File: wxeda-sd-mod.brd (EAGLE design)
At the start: 101.3 x 40.6 mm, 23 parts, among them U1 SD_CARD, X2 TAPE IN / OUT

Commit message: release
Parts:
- C2, C3, C4, C5: device adafruit:E5-8,5 -> adafruit:E2-5
- moved C3 8.98 mm to (72.4, 24.1), turned to 0 degrees
- moved R7 6.48 mm to (68.6, 16.5), turned to 0 degrees
- moved C2 1.80 mm to (85.1, 24.1)
- moved C5 1.80 mm to (92.7, 24.1)
- moved C4 1.27 mm to (64.8, 24.1), turned to 0 degrees
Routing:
- net Y_OUT: track 16.7 -> 11.4 mm
- net N$8: track 12.7 -> 8.25 mm
- net DSE: track 40.1 -> 44.2 mm
- net N$7: track 8.89 -> 5.05 mm
- net N$4: track 11.3 -> 9.23 mm
- net A_IN: track 15.2 -> 16.8 mm
- net C_OUT: track 9.73 -> 11.1 mm
- net N$6: track 11.2 -> 10.2 mm
- net GREEN: track 26.5 -> 25.4 mm
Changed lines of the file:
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@@
 <elements>
 <element name="JP1" library="pinhead" package="1X06" value="7SEG_LR" x="45.72" y="30.48" smashed="yes">
-<attribute name="NAME" x="49.4538" y="27.2288" size="1.27" layer="25" ratio="10"/>
+<attribute name="NAME" x="39.2938" y="27.2288" size="0.8128" layer="25" ratio="10"/>
 </element>
 <element name="JP2" library="pinhead" package="1X03" value="IRDA" x="77.47" y="35.56" smashed="yes" rot="R180"/>
 <element name="U1" library="SparkFun-Connectors" package="SDCARD_4UCONN" value="SD_CARD" x="21.59" y="11.43" smashed="yes" rot="R90">
-<attribute name="VALUE" x="17.54" y="22.13" size="1.27" layer="27" ratio="10"/>
+<attribute name="VALUE" x="8.65" y="13.24" size="0.8128" layer="27" ratio="10"/>
 </element>
 <element name="JP3" library="pinhead" package="1X06" value="7SEG_HR" x="45.72" y="38.1" smashed="yes"/>
@@
 <attribute name="NAME" x="43.18" y="11.43" size="0.8128" layer="25" font="vector" rot="R180"/>
 </element>
-<element name="C2" library="adafruit" package="E5-8,5" value="10uF" x="83.82" y="22.86" smashed="yes" rot="R180">
-<attribute name="NAME" x="84.7598" y="18.034" size="1.27" layer="25" ratio="10" rot="R180"/>
-<attribute name="VALUE" x="86.3346" y="25.8826" size="1.27" layer="27" ratio="10" rot="R180"/>
+<element name="C2" library="adafruit" package="E2-5" value="10uF" x="85.09" y="24.13" smashed="yes" rot="R180">
+<attribute name="NAME" x="87.2998" y="20.574" size="0.8128" layer="25" ratio="10" rot="R180"/>
 </element>
 <element name="R9" library="SparkFun-Passives" package="AXIAL-0.3" value="75" x="55.88" y="26.67" smashed="yes">
-<attribute name="NAME" x="53.34" y="29.2354" size="0.8128" layer="25" rot="R270"/>
-</element>
-<element name="C4" library="adafruit" package="E5-8,5" value="47uF" x="66.04" y="24.13" smashed="yes" rot="R90">
-<attribute name="NAME" x="63.754" y="23.1902" size="1.27" layer="25" ratio="10" rot="R90"/>
-<attribute name="VALUE" x="69.0626" y="21.6154" size="1.27" layer="27" ratio="10" rot="R90"/>
-</element>
-<element name="X2" library="adafruit" package="STX3100" value="TAPE IN / OUT" x="88.9" y="40.64" smashed="yes" rot="R270">
-<attribute name="VALUE" x="82.45" y="27.86" size="1.27" layer="27" ratio="10"/>
-</element>
-<element name="C5" library="adafruit" package="E5-8,5" value="10uF" x="93.98" y="22.86" smashed="yes" rot="R180">
-<attribute name="NAME" x="94.9198" y="18.034" size="1.27" layer="25" ratio="10" rot="R180"/>
-<attribute name="VALUE" x="96.4946" y="25.8826" size="1.27" layer="27" ratio="10" rot="R180"/>
-</element>
-<element name="R7" library="SparkFun-Passives" package="AXIAL-0.3" value="75" x="62.23" y="15.24" rot="R270"/>
-<element name="C3" library="adafruit" package="E5-8,5" value="47uF" x="73.66" y="15.24" rot="R90"/>
+<attribute name="NAME" x="57.15" y="24.1554" size="0.8128" layer="25"/>
+</element>
+<element name="C4" library="adafruit" package="E2-5" value="47uF" x="64.77" y="24.13" smashed="yes">
+<attribute name="NAME" x="67.6402" y="21.336" size="0.8128" layer="25" rot="R180"/>
+</element>
+<element name="X2" library="adafruit" package="STX3100" value="TAPE IN / OUT" x="88.9" y="40.64" smashed="yes" rot="R270"/>
+<element name="C5" library="adafruit" package="E2-5" value="10uF" x="92.71" y="24.13" smashed="yes" rot="R180">
+<attribute name="NAME" x="94.9198" y="20.574" size="0.8128" layer="25" ratio="10" rot="R180"/>
+</element>
+<element name="R7" library="SparkFun-Passives" package="AXIAL-0.3" value="75" x="68.58" y="16.51" smashed="yes">
+<attribute name="NAME" x="69.85" y="13.97" size="0.8128" layer="25" font="vector"/>
+</element>
+<element name="C3" library="adafruit" package="E2-5" value="47uF" x="72.39" y="24.13" smashed="yes">
+<attribute name="NAME" x="74.93" y="21.336" size="0.8128" layer="25" ratio="10" rot="R180"/>
+</element>
 <element name="U$1" library="connectors-digital" package="MINIDIN_4_3GND" value="S-VIDEO" x="63.5" y="43.18">
 <attribute name="PACKAGE" value="SHIELDED" x="63.5" y="43.18" size="1.778" layer="27" display="off"/>
@@
 <wire x1="58.42" y1="7.62" x2="58.42" y2="11.43" width="1.016" layer="1"/>
 <wire x1="58.42" y1="11.43" x2="58.42" y2="13.97" width="1.016" layer="1"/>
-<wire x1="58.42" y1="13.97" x2="58.42" y2="15.24" width="0" layer="19" extent="1-16"/>
 <wire x1="58.42" y1="13.97" x2="58.42" y2="16.51" width="1.016" layer="1"/>
 <wire x1="58.42" y1="16.51" x2="58.42" y2="19.05" width="1.016" layer="1"/>
@@
 <wire x1="54.61" y1="13.97" x2="58.42" y2="13.97" width="0.8128" layer="1"/>
 <wire x1="52.07" y1="11.43" x2="58.42" y2="11.43" width="0.8128" layer="1"/>
-<wire x1="62.23" y1="15.24" x2="58.42" y2="15.24" width="0" layer="19" extent="1-16"/>
 <wire x1="74.93" y1="35.56" x2="74.93" y2="33.02" width="1.016" layer="1"/>
 <wire x1="74.93" y1="33.02" x2="77.47" y2="30.48" width="1.016" layer="1"/>
@@
 <contactref element="JP1" pad="1"/>
 <contactref element="R7" pad="P$1"/>
-<wire x1="62.23" y1="19.05" x2="59.69" y2="22.86" width="0.6096" layer="1"/>
-<wire x1="59.69" y1="22.86" x2="55.88" y2="22.86" width="0.6096" layer="1"/>
+<wire x1="64.77" y1="16.51" x2="60.96" y2="22.86" width="0.6096" layer="1"/>
+<wire x1="60.96" y1="22.86" x2="55.88" y2="22.86" width="0.6096" layer="1"/>
 <wire x1="55.88" y1="22.86" x2="55.88" y2="34.29" width="0.6096" layer="1"/>
 <wire x1="55.88" y1="34.29" x2="39.37" y2="34.29" width="0.6096" layer="1"/>
@@
 <contactref element="C5" pad="+"/>
 <wire x1="99.06" y1="35.56" x2="96.52" y2="35.56" width="0.8128" layer="1"/>
-<wire x1="96.52" y1="35.56" x2="96.52" y2="22.86" width="0.8128" layer="1"/>
+<wire x1="96.52" y1="35.56" x2="96.52" y2="24.13" width="0.6096" layer="1"/>
+<wire x1="96.52" y1="24.13" x2="93.726" y2="24.13" width="0.6096" layer="1"/>
 </signal>
 <signal name="GREEN">
 <contactref element="JP4" pad="3"/>
 <contactref element="C2" pad="+"/>
-<wire x1="86.36" y1="22.86" x2="88.9" y2="20.32" width="0.8128" layer="1"/>
-<wire x1="88.9" y1="20.32" x2="99.06" y2="20.32" width="0.8128" layer="1"/>
-<wire x1="99.06" y1="20.32" x2="99.06" y2="33.02" width="0.8128" layer="1"/>
+<wire x1="86.106" y1="24.13" x2="88.646" y2="21.59" width="0.6096" layer="1"/>
+<wire x1="88.646" y1="21.59" x2="99.06" y2="21.59" width="0.6096" layer="1"/>
+<wire x1="99.06" y1="21.59" x2="99.06" y2="33.02" width="0.6096" layer="1"/>
 </signal>
 <signal name="N$1">
@@
 <contactref element="C2" pad="-"/>
 <wire x1="83.7" y1="32.94" x2="83.82" y2="32.94" width="0.6096" layer="1"/>
-<wire x1="83.82" y1="32.94" x2="83.82" y2="25.4" width="0.8128" layer="1"/>
-<wire x1="83.82" y1="25.4" x2="81.28" y2="22.86" width="0.8128" layer="1"/>
+<wire x1="83.7" y1="32.94" x2="83.82" y2="32.82" width="0.6096" layer="1"/>
+<wire x1="83.82" y1="32.82" x2="83.82" y2="24.13" width="0.6096" layer="1"/>
+<wire x1="83.82" y1="24.13" x2="84.074" y2="24.13" width="0.6096" layer="1"/>
 </signal>
 <signal name="N$6">
@@
 <contactref element="C5" pad="-"/>
 <wire x1="93.9" y1="32.94" x2="93.98" y2="32.94" width="0.8128" layer="1"/>
-<wire x1="93.98" y1="32.94" x2="93.98" y2="25.4" width="0.8128" layer="1"/>
-<wire x1="93.98" y1="25.4" x2="91.44" y2="22.86" width="0.8128" layer="1"/>
+<wire x1="93.9" y1="32.94" x2="92.71" y2="31.75" width="0.6096" layer="1"/>
+<wire x1="92.71" y1="31.75" x2="92.71" y2="27.94" width="0.6096" layer="1"/>
+<wire x1="92.71" y1="27.94" x2="91.44" y2="26.67" width="0.6096" layer="1"/>
+<wire x1="91.44" y1="26.67" x2="91.44" y2="24.13" width="0.6096" layer="1"/>
+<wire x1="91.44" y1="24.13" x2="91.694" y2="24.13" width="0.6096" layer="1"/>
 </signal>
 <signal name="N$7">
 <contactref element="R9" pad="P$2"/>
 <contactref element="C4" pad="+"/>
-<wire x1="59.69" y1="26.67" x2="62.23" y2="26.67" width="0.6096" layer="1"/>
-<wire x1="62.23" y1="26.67" x2="66.04" y2="21.59" width="0.6096" layer="1"/>
+<wire x1="59.69" y1="26.67" x2="60.96" y2="25.4" width="0.6096" layer="1"/>
+<wire x1="60.96" y1="25.4" x2="62.23" y2="25.4" width="0.6096" layer="1"/>
+<wire x1="62.23" y1="25.4" x2="62.484" y2="25.146" width="0.6096" layer="1"/>
+<wire x1="62.484" y1="25.146" x2="63.754" y2="24.13" width="0.6096" layer="1"/>
 </signal>
 <signal name="Y_OUT">
 <contactref element="U$1" pad="3"/>
 <contactref element="C3" pad="-"/>
-<wire x1="67.8" y1="32.18" x2="73.66" y2="25.83" width="0.6096" layer="1"/>
-<wire x1="73.66" y1="25.83" x2="73.66" y2="17.78" width="0.6096" layer="1"/>
+<wire x1="67.8" y1="32.18" x2="70.77" y2="27.94" width="0.6096" layer="1"/>
+<wire x1="70.77" y1="27.94" x2="72.39" y2="27.94" width="0.6096" layer="1"/>
+<wire x1="72.39" y1="27.94" x2="73.66" y2="26.67" width="0.6096" layer="1"/>
+<wire x1="73.66" y1="26.67" x2="73.66" y2="24.13" width="0.6096" layer="1"/>
+<wire x1="73.66" y1="24.13" x2="73.406" y2="24.13" width="0.6096" layer="1"/>
 </signal>
 <signal name="N$8">
 <contactref element="R7" pad="P$2"/>
 <contactref element="C3" pad="+"/>
-<wire x1="73.66" y1="12.7" x2="62.23" y2="12.7" width="0.6096" layer="1"/>
-<wire x1="62.23" y1="12.7" x2="62.23" y2="11.43" width="0.6096" layer="1"/>
+<wire x1="71.374" y1="24.13" x2="71.12" y2="23.876" width="0.6096" layer="1"/>
+<wire x1="71.12" y1="23.876" x2="71.12" y2="17.78" width="0.6096" layer="1"/>
+<wire x1="71.12" y1="17.78" x2="72.39" y2="16.51" width="0.6096" layer="1"/>
 </signal>
 <signal name="C_OUT">
 <contactref element="U$1" pad="4"/>
 <contactref element="C4" pad="-"/>
-<wire x1="59.2" y1="32.18" x2="62.23" y2="32.18" width="0.6096" layer="1"/>
-<wire x1="62.23" y1="32.18" x2="66.04" y2="26.67" width="0.6096" layer="1"/>
+<wire x1="59.2" y1="32.18" x2="62.17" y2="29.21" width="0.6096" layer="1"/>
+<wire x1="62.17" y1="29.21" x2="62.23" y2="27.94" width="0.6096" layer="1"/>
+<wire x1="62.23" y1="27.94" x2="66.04" y2="24.13" width="0.6096" layer="1"/>
+<wire x1="66.04" y1="24.13" x2="65.786" y2="24.13" width="0.6096" layer="1"/>
 </signal>
 </signals>

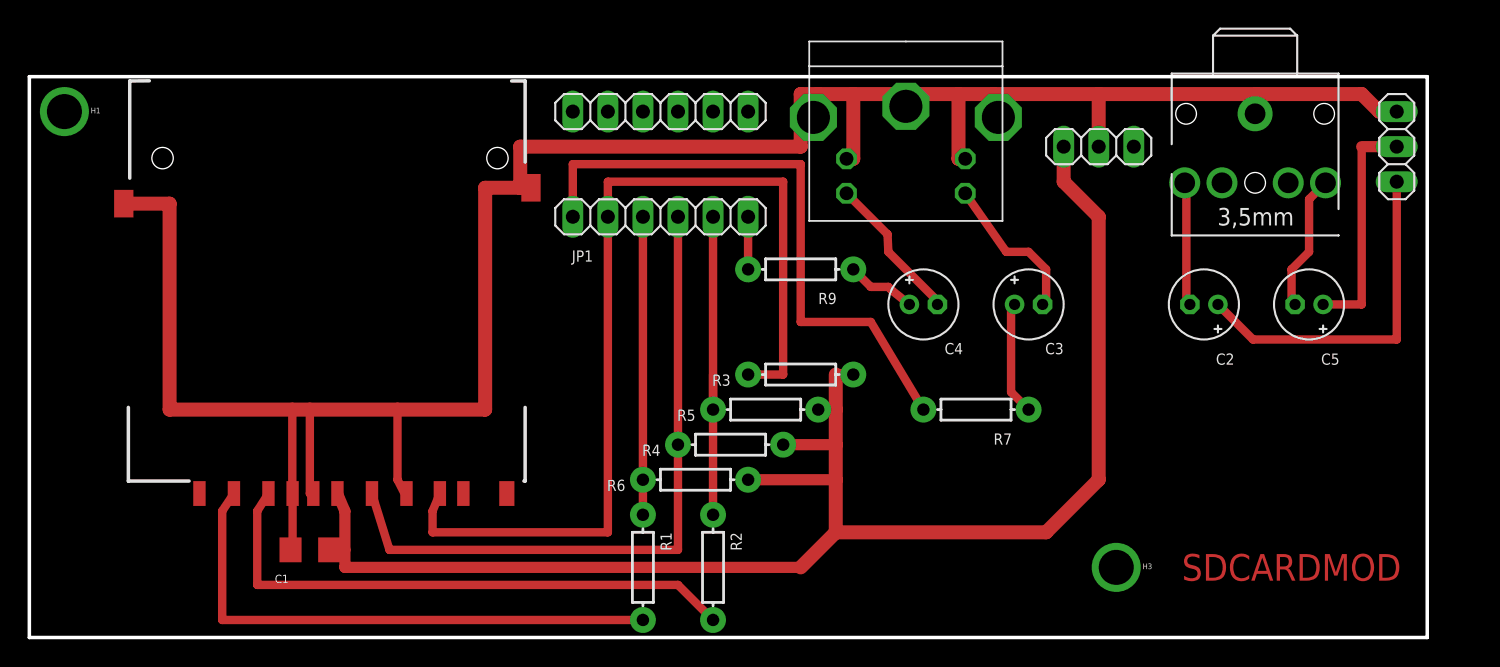
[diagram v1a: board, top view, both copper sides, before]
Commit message: Added stereo output
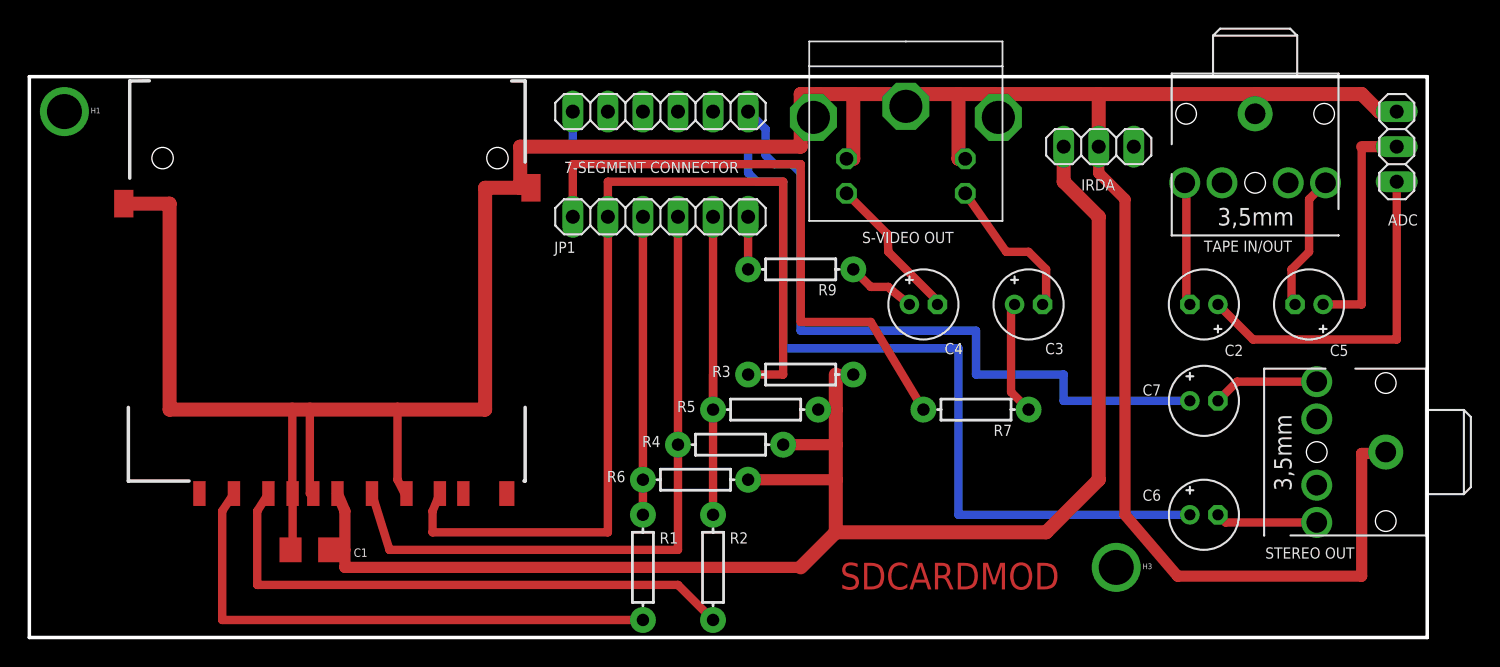
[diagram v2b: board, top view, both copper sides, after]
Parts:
- added C6, C7: 10uF, adafruit:E2-5
- added X1: STEREO OUT, adafruit:STX3100
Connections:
- new net N$10: C7.-, X1.5
- new net N$5: C6.-, X1.2
- net DSB: now also C7.+
- net DSEN1: now also C6.+
- net GND: now also X1.1
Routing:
- net DSEN1: track 0.00 -> 73.5 mm
- net GND: track 175.4 -> 232.7 mm
- net DSB: track 0.00 -> 51.5 mm
- net N$10: track 0.00 -> 7.73 mm
- net N$5: track 0.00 -> 7.39 mm
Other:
- board text added: "7-SEGMENT CONNECTOR"
- board text added: "ADC"
- board text added: "IRDA"
- board text added: "S-VIDEO OUT"
- board text added: "STEREO OUT"
- board text added: "TAPE IN/OUT"
